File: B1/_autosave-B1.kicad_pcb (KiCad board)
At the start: 4 copper layers, 100 x 100 mm, 15 parts, among them U1 74HC04, U2 74HC00, U3 74HC32, U4 74HC377, U5 74HC244, U6 74HC74, U7 74HC74, U8 74HC08

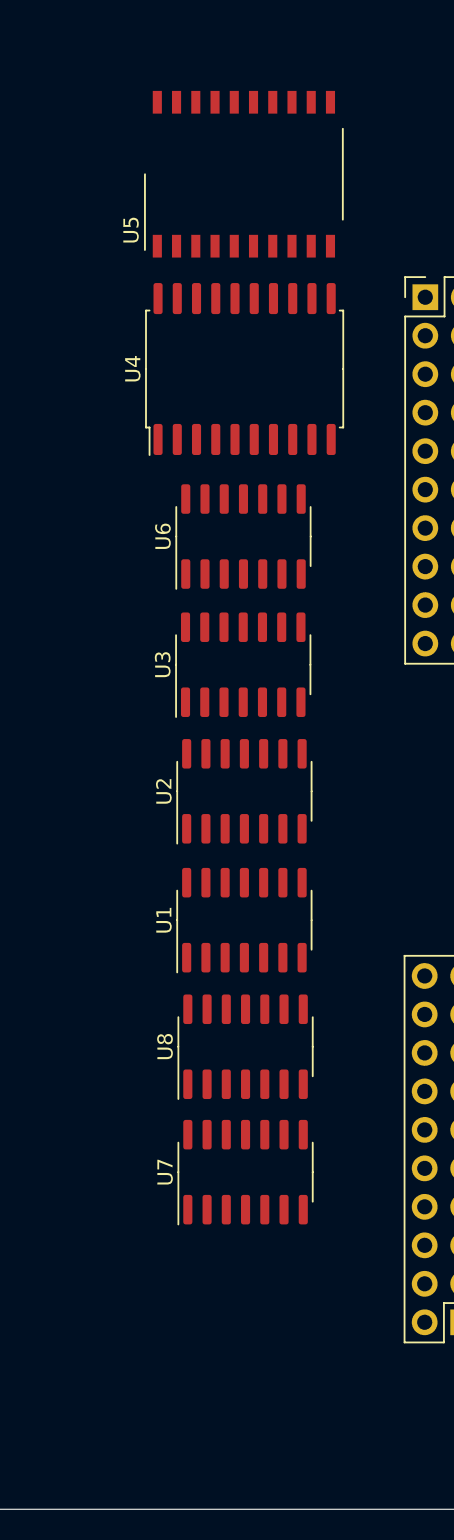
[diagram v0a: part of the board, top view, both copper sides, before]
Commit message: B1 CREGA added
Work started on b1. CREGA added.
Minor changes to B0 schematic properties.
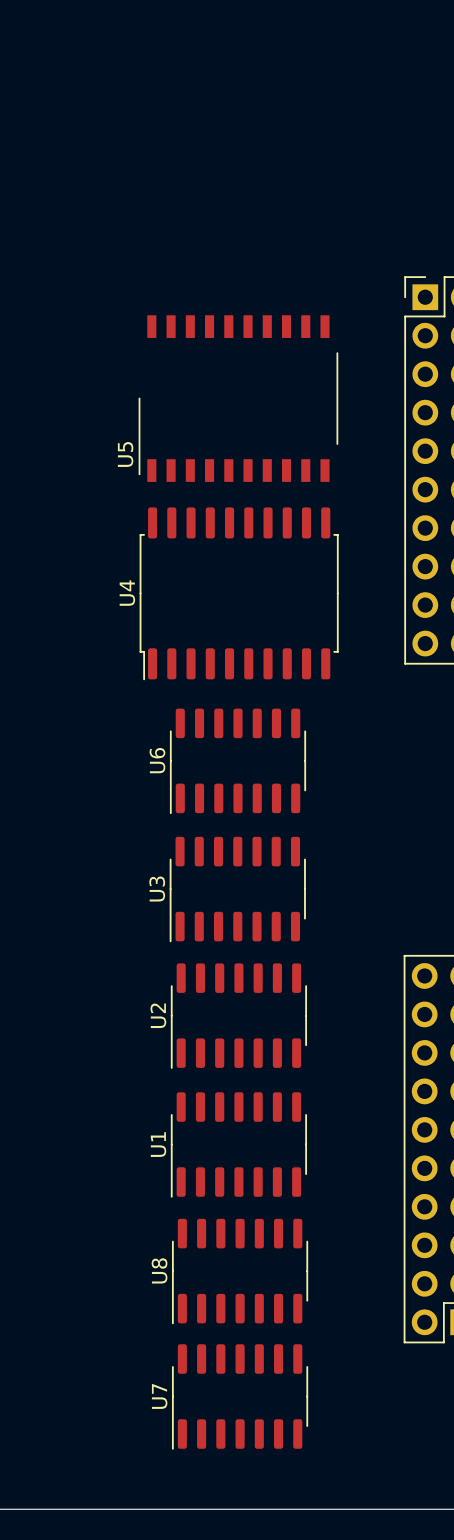
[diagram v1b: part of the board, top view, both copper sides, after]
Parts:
- moved U1 14.8 mm to (177.7, 120.9)
- moved U8 14.8 mm to (177.8, 129.3)
- moved U4 14.8 mm to (177.7, 84.5)
- moved U2 14.8 mm to (177.7, 112.4)
- moved U3 14.8 mm to (177.6, 104.1)
- moved U6 14.8 mm to (177.6, 95.6)
- moved U7 14.8 mm to (177.8, 137.6)
- moved U5 14.8 mm to (177.7, 71.7)
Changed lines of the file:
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@@
   (net 108 "Net-(U7-Pad2)")
   (footprint "Package_SO:SOIC-14_3.9x8.7mm_P1.27mm" (layer "F.Cu")
-    (at 177.983 89.257 90)
+    (at 177.622 104.066 90)
     (descr "SOIC, 14 Pin (JEDEC MS-012AB, https://www.analog.com/media/en/package-pcb-resources/package/pkg_pdf/soic_narrow-r/r_14.pdf), generated with kicad-footprint-generator ipc_gullwing_generator.py")
     (tags "SOIC SO")
@@
   )
   (footprint "Package_SO:SOIC-14_3.9x8.7mm_P1.27mm" (layer "F.Cu")
-    (at 178.059 97.611 90)
+    (at 177.698 112.42 90)
     (descr "SOIC, 14 Pin (JEDEC MS-012AB, https://www.analog.com/media/en/package-pcb-resources/package/pkg_pdf/soic_narrow-r/r_14.pdf), generated with kicad-footprint-generator ipc_gullwing_generator.py")
     (tags "SOIC SO")
@@
   )
   (footprint "Package_SO:SOIC-14_3.9x8.7mm_P1.27mm" (layer "F.Cu")
-    (at 178.059 106.118 90)
+    (at 177.698 120.927 90)
     (descr "SOIC, 14 Pin (JEDEC MS-012AB, https://www.analog.com/media/en/package-pcb-resources/package/pkg_pdf/soic_narrow-r/r_14.pdf), generated with kicad-footprint-generator ipc_gullwing_generator.py")
     (tags "SOIC SO")
@@
   )
   (footprint "Package_SO:SO-20_12.8x7.5mm_P1.27mm" (layer "F.Cu")
-    (at 178.026 56.88 90)
+    (at 177.665 71.689 90)
     (descr "SO-20, 12.8x7.5mm, https://www.nxp.com/docs/en/data-sheet/SA605.pdf")
     (tags "S0-20 ")
@@
   )
   (footprint "Package_SO:SO-14_3.9x8.65mm_P1.27mm" (layer "F.Cu")
-    (at 177.998 80.795 90)
+    (at 177.637 95.604 90)
     (descr "SO, 14 Pin (https://www.st.com/resource/en/datasheet/l6491.pdf), generated with kicad-footprint-generator ipc_gullwing_generator.py")
     (tags "SO SO")
@@
   )
   (footprint "Package_SO:SO-14_3.9x8.65mm_P1.27mm" (layer "F.Cu")
-    (at 178.135 114.473 90)
+    (at 177.774 129.282 90)
     (descr "SO, 14 Pin (https://www.st.com/resource/en/datasheet/l6491.pdf), generated with kicad-footprint-generator ipc_gullwing_generator.py")
     (tags "SO SO")
@@
   )
   (footprint "Package_SO:SOIC-20W_7.5x12.8mm_P1.27mm" (layer "F.Cu")
-    (at 178.074 69.738 90)
+    (at 177.713 84.547 90)
     (descr "SOIC, 20 Pin (JEDEC MS-013AC, https://www.analog.com/media/en/package-pcb-resources/package/233848rw_20.pdf), generated with kicad-footprint-generator ipc_gullwing_generator.py")
     (tags "SOIC SO")
@@
   )
   (footprint "Package_SO:SO-14_3.9x8.65mm_P1.27mm" (layer "F.Cu")
-    (at 178.135 122.751 90)
+    (at 177.774 137.56 90)
     (descr "SO, 14 Pin (https://www.st.com/resource/en/datasheet/l6491.pdf), generated with kicad-footprint-generator ipc_gullwing_generator.py")
     (tags "SO SO")
